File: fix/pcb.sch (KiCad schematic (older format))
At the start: 20 parts

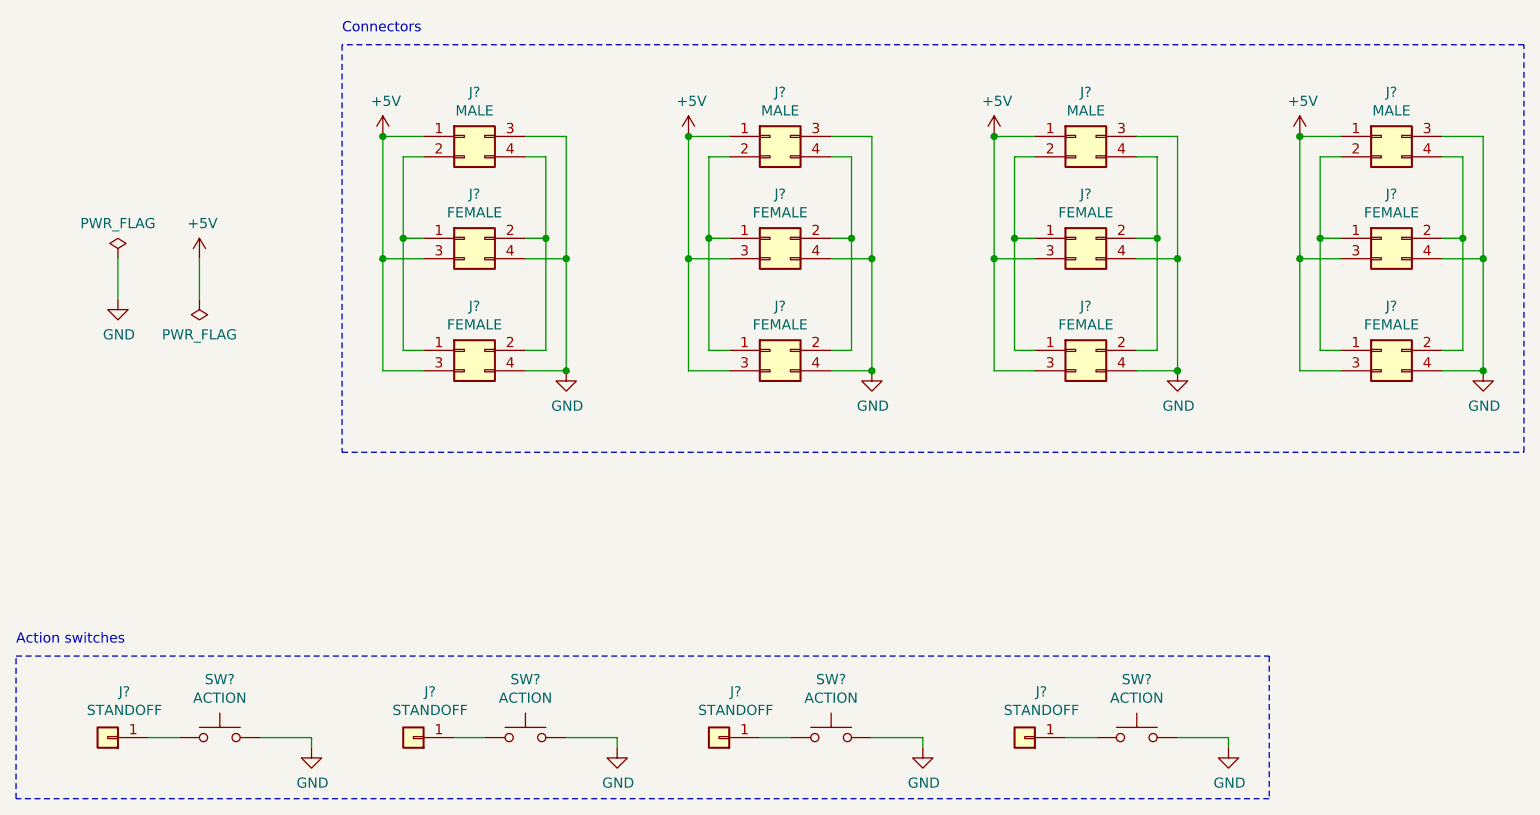
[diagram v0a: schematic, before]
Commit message: Fix fix: Wrong wiring for new males
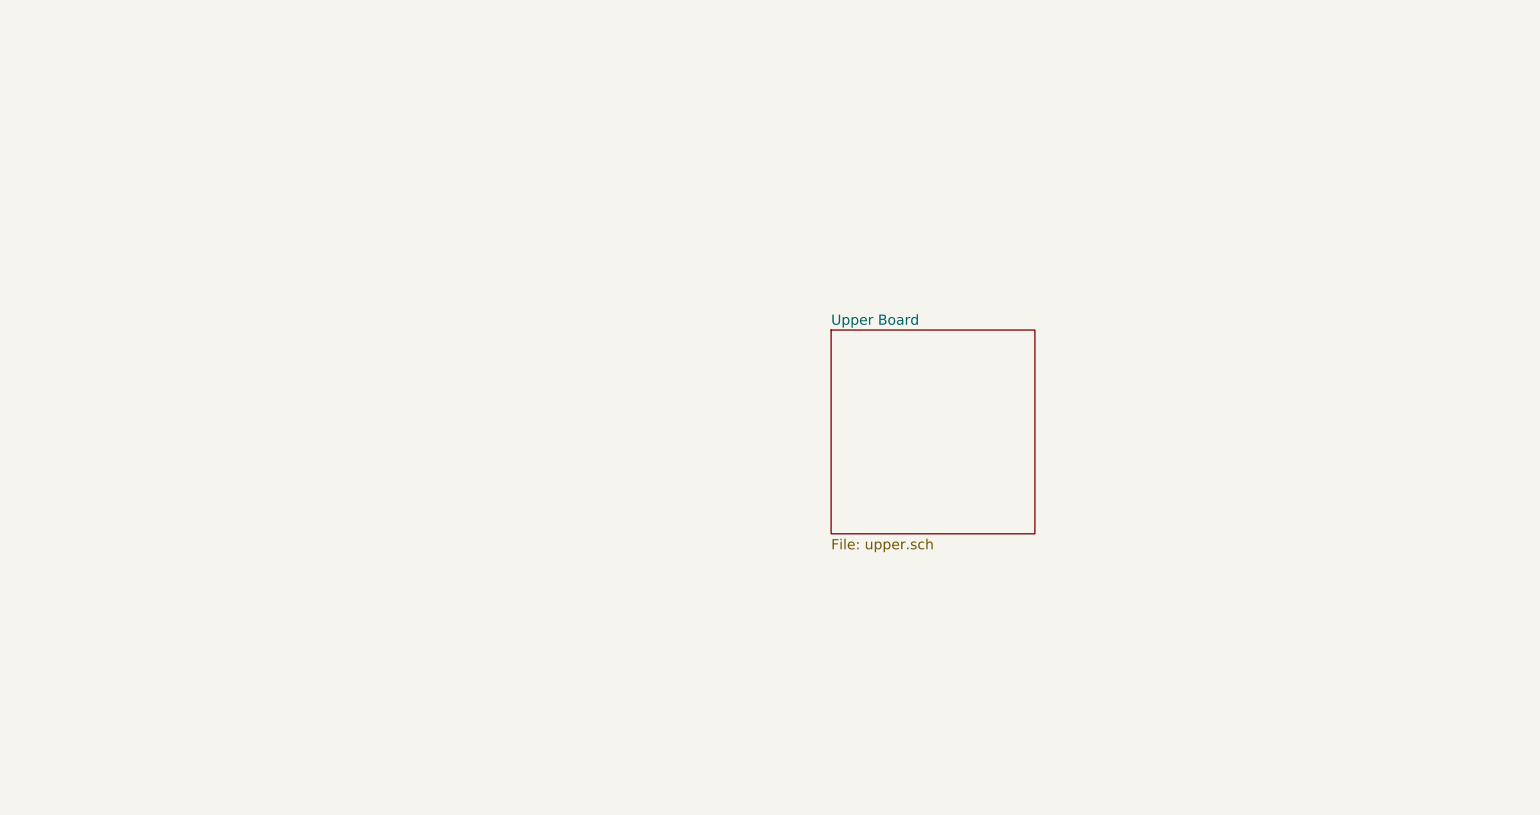
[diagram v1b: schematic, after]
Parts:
- removed J? (x4): STANDOFF, MountingHole:MountingHole_2.2mm_M2_Pad_Via, symbol Connector_Generic:Conn_01x01
- removed J? (x8): FEMALE, Connector_PinSocket_2.54mm:PinSocket_2x02_P2.54mm_Horizontal, symbol Connector_Generic:Conn_02x02_Odd_Even
- removed J? (x4): MALE, Connector_PinHeader_2.54mm:PinHeader_2x02_P2.54mm_Horizontal, symbol Connector_Generic:Conn_02x02_Top_Bottom
- removed SW? (x4): ACTION, node:top-leaf, symbol Switch:SW_Push
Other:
- note removed: "Action switches"
- note removed: "Connectors"

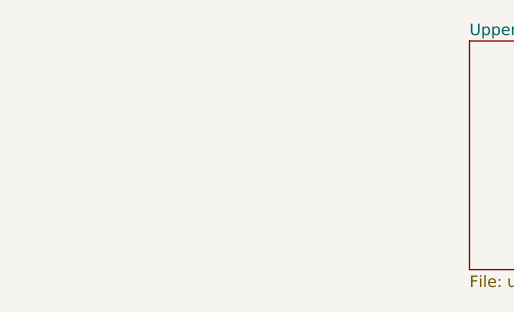
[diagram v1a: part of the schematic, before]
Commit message: Add mounting holes for PCBA
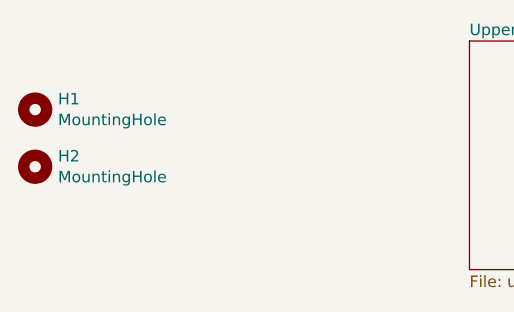
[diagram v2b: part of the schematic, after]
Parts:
- added H1, H2: MountingHole, node:JLCPCB-tooling-hole, symbol Mechanical:MountingHole
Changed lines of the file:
@@
 F1 "upper.sch" 50
 $EndSheet
+$Comp
+L Mechanical:MountingHole H1
+U 1 1 5FC5FBD1
+P 4100 3300
+F 0 "H1" H 4200 3346 50  0000 L CNN
+F 1 "MountingHole" H 4200 3255 50  0000 L CNN
+F 2 "node:JLCPCB-tooling-hole" H 4100 3300 50  0001 C CNN
+F 3 "~" H 4100 3300 50  0001 C CNN
+	1    4100 3300
+	1    0    0    -1
+$EndComp
+$Comp
+L Mechanical:MountingHole H2
+U 1 1 5FC5FD0A
+P 4100 3550
+F 0 "H2" H 4200 3596 50  0000 L CNN
+F 1 "MountingHole" H 4200 3505 50  0000 L CNN
+F 2 "node:JLCPCB-tooling-hole" H 4100 3550 50  0001 C CNN
+F 3 "~" H 4100 3550 50  0001 C CNN
+	1    4100 3550
+	1    0    0    -1
+$EndComp
 $EndSCHEMATC
